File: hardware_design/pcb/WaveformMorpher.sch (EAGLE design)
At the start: 52 parts, among them IC1 MAX11615EEE+, IC2 TL074D, IC3 LM4041B12DBZ, J1 WQP-PJ301M-12_JACK, J2 WQP-PJ301M-12_JACK, J3 WQP-PJ301M-12_JACK, J4 WQP-PJ301M-12_JACK, J5 WQP-PJ301M-12_JACK, T1 MMBT3904

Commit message: Board added
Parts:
- added C10, C11, C12, C7, C8, C9: 100n, rcl:C-USC0603
- added C5: 10u, rcl:CPOL-USB
- added C6: 18p, rcl:C-USC0603
- added IC4: LME49720MAX_NOPB, SamacSys_Parts:LME49720MAX_NOPB
- added J6: OUT_J, MusicThingModular:WQP-PJ301M-12_JACK
- added R24: 6.8k, rcl:R-US_R0603
- added R25, R27: 47k, rcl:R-US_R0603
- added R26: 1.0k, rcl:R-US_R0603
- added VR1: LOOP_CV_POT, MusicThingModular:9MM_SNAP-IN_POT_
- J1: value WQP-PJ301M-12_JACK -> GATE_J
- J2: value WQP-PJ301M-12_JACK -> MORPH_J
- J3: value WQP-PJ301M-12_JACK -> 1V/OCT_J
- J4: value WQP-PJ301M-12_JACK -> LOOP_J
- J5: value WQP-PJ301M-12_JACK -> RASP_IN_J
- VR5: value (none) -> LOOP_POT
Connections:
- removed net 12V: D1.K
- new net +12V: C11.1, D1.K, IC4.V+
- new net N$17: IC4.INPUT_B-, IC4.OUTPUT_B
- new net N$18: C6.2, IC4.OUTPUT_A, R26.1, R27.2
- new net N$19: J5.2, R26.2
- new net N$2: C10.1, C7.1, C8.1, C9.1
- new net N$20: C5.+, J6.2
- new net N$21: C5.-, R24.1, R25.2
- new net N$22: R20.1, VR5.S
- new net N$23: C6.1, IC4.INPUT_A-, R24.2, R27.1
- new net N$24: R23.1, VR1.S
- new net N$3: IC1.REF, IC2A.+IN
- net -12V: now also C12.2, IC4.V-
- net 5V: now also J4.3
- net GND: now also C10.2, C11.2, C12.1, C7.2, C8.2, C9.2, IC2D.+IN, IC4.INPUT_A+, IC4.INPUT_B+, J6.1, R25.1, VR1.A, VR5.A
- net N$12: now also J2.1
- net N$16: now also VR1.E; no longer R23.1
- net VREF2.0: now also IC2A.-IN, IC2A.OUT, VR5.E; no longer IC1.REF, R20.1
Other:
- moved on the sheet: ATTACK_POT, C1, C2, C3, C4, D1, D2, DECAY_POT, IC1, IC2B, IC2C, IC2D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

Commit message: Board first placements
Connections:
- removed net 1V/OCT_ADC1: C3.2, R18.2
- net MORPH_ADC: now also C3.2, R18.2
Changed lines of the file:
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@@
-</segment>
-</net>
-<net name="1V/OCT_ADC1" class="0">
-<segment>
-<pinref part="C3" gate="G$1" pin="2"/>
-<wire x1="76.2" y1="121.92" x2="83.82" y2="121.92" width="0.1524" layer="91"/>
-<wire x1="83.82" y1="121.92" x2="83.82" y2="111.76" width="0.1524" layer="91"/>
-<pinref part="R18" gate="G$1" pin="2"/>
-<wire x1="83.82" y1="111.76" x2="76.2" y2="111.76" width="0.1524" layer="91"/>
-<wire x1="83.82" y1="111.76" x2="83.82" y2="99.06" width="0.1524" layer="91"/>
-<junction x="83.82" y="111.76"/>
 </segment>
 </net>
@@
 <junction x="58.42" y="101.6"/>
 <pinref part="IC2" gate="C" pin="-IN"/>
-</segment>
-</net>
-<net name="MORPH_ADC" class="0">
-<segment>
-<pinref part="IC2" gate="C" pin="OUT"/>
-<wire x1="78.74" y1="99.06" x2="88.9" y2="99.06" width="0.1524" layer="91"/>
-<label x="88.9" y="99.06" size="1.778" layer="95" xref="yes"/>
 </segment>
 </net>
@@
 </segment>
 </net>
+<net name="MORPH_ADC" class="0">
+<segment>
+<pinref part="C3" gate="G$1" pin="2"/>
+<wire x1="76.2" y1="121.92" x2="83.82" y2="121.92" width="0.1524" layer="91"/>
+<wire x1="83.82" y1="121.92" x2="83.82" y2="111.76" width="0.1524" layer="91"/>
+<pinref part="R18" gate="G$1" pin="2"/>
+<wire x1="83.82" y1="111.76" x2="76.2" y2="111.76" width="0.1524" layer="91"/>
+<pinref part="IC2" gate="C" pin="OUT"/>
+<wire x1="78.74" y1="99.06" x2="83.82" y2="99.06" width="0.1524" layer="91"/>
+<label x="88.9" y="99.06" size="1.778" layer="95" xref="yes"/>
+<wire x1="83.82" y1="99.06" x2="88.9" y2="99.06" width="0.1524" layer="91"/>
+<wire x1="83.82" y1="111.76" x2="83.82" y2="99.06" width="0.1524" layer="91"/>
+<junction x="83.82" y="111.76"/>
+<junction x="83.82" y="99.06"/>
+</segment>
+</net>

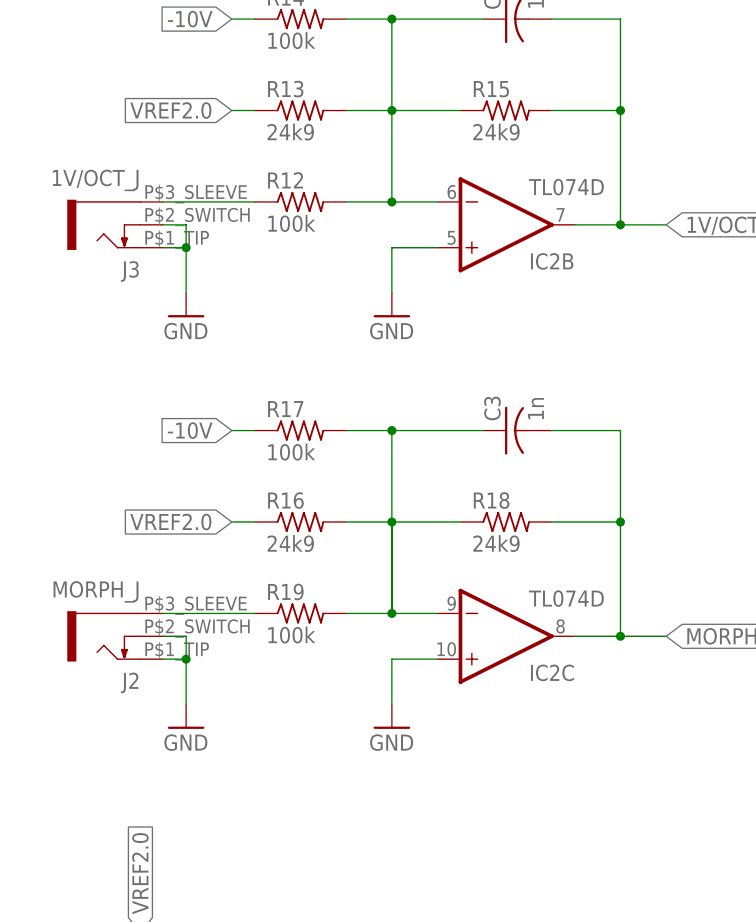
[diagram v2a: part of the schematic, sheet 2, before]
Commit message: adding vias
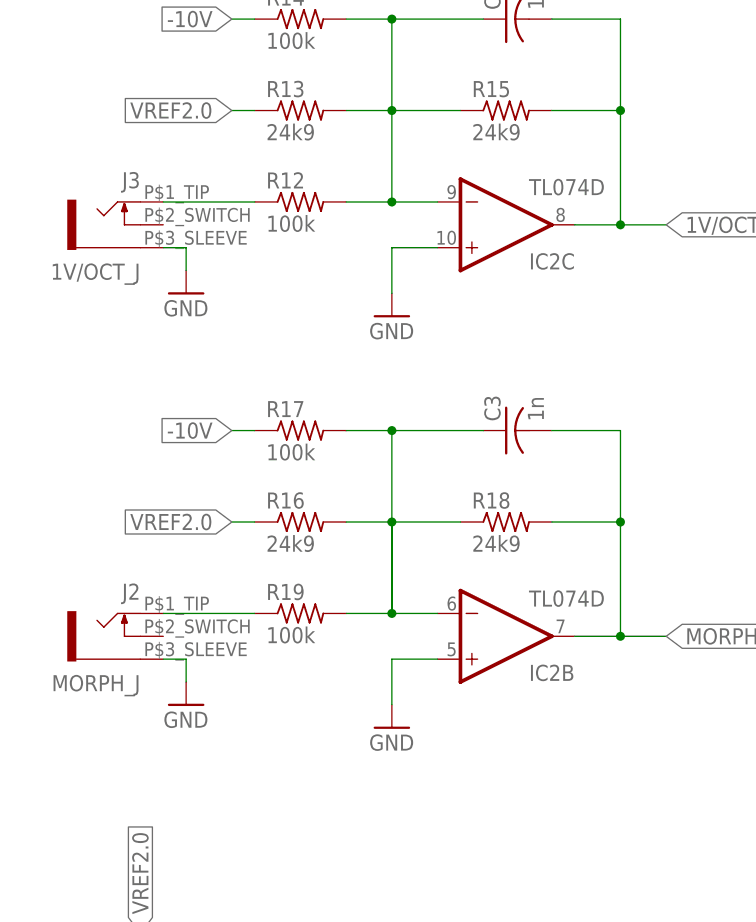
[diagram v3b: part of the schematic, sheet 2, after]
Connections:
- removed net N$13: IC2C.-IN, R19.2
- net 1V/OCT_ADC: now also IC2C.OUT; no longer IC2B.OUT
- net GND: now also J2.1, J3.1; no longer J2.2, J2.3, J3.2, J3.3
- net MORPH_ADC: now also IC2B.OUT; no longer IC2C.OUT
- net N$10: now also IC2B.-IN, R19.2
- net N$12: now also J3.2, R12.1; no longer J2.1, R19.1
- net N$8: now also J2.2, R19.1; no longer J3.1, R12.1
- net N$9: now also IC2C.-IN; no longer IC2B.-IN
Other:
- moved on the sheet: IC2B, IC2C, J2, J3
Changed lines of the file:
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@@
 <part name="GND5" library="supply1" deviceset="GND" device=""/>
 <part name="GND6" library="supply1" deviceset="GND" device=""/>
-<part name="GND7" library="supply1" deviceset="GND" device=""/>
-<part name="GND8" library="supply1" deviceset="GND" device=""/>
 <part name="GND9" library="supply1" deviceset="GND" device=""/>
 <part name="GND10" library="supply1" deviceset="GND" device=""/>
@@
 <part name="VR1" library="MusicThingModular" deviceset="9MM_SNAP-IN_POT" device="_" value="LOOP_CV_POT"/>
 <part name="GND36" library="supply1" deviceset="GND" device=""/>
+<part name="GND7" library="supply1" deviceset="GND" device=""/>
+<part name="GND8" library="supply1" deviceset="GND" device=""/>
 </parts>
 <sheets>
@@
 <instances>
 <instance part="J5" gate="G$1" x="124.46" y="78.74" rot="MR0"/>
-<instance part="J3" gate="G$1" x="27.94" y="144.78" rot="R180"/>
-<instance part="J2" gate="G$1" x="27.94" y="99.06" rot="R180"/>
+<instance part="J3" gate="G$1" x="27.94" y="144.78" rot="MR0"/>
+<instance part="J2" gate="G$1" x="27.94" y="99.06" rot="MR0"/>
 <instance part="J1" gate="G$1" x="200.66" y="116.84" rot="MR0"/>
 <instance part="J4" gate="G$1" x="25.4" y="33.02" rot="MR0"/>
@@
 <instance part="GND5" gate="1" x="134.62" y="68.58" rot="MR0"/>
 <instance part="GND6" gate="1" x="33.02" y="22.86"/>
-<instance part="GND7" gate="1" x="35.56" y="134.62"/>
-<instance part="GND8" gate="1" x="35.56" y="88.9"/>
 <instance part="GND9" gate="1" x="208.28" y="106.68"/>
-<instance part="IC2" gate="B" x="71.12" y="144.78" rot="MR180"/>
-<instance part="IC2" gate="C" x="71.12" y="99.06" rot="MR180"/>
+<instance part="IC2" gate="B" x="71.12" y="99.06" rot="MR180"/>
+<instance part="IC2" gate="C" x="71.12" y="144.78" rot="MR180"/>
 <instance part="IC2" gate="D" x="86.36" y="33.02" rot="MR180"/>
 <instance part="I/O" gate="G$1" x="-5.08" y="0">
@@
 <instance part="VR1" gate="G$1" x="48.26" y="30.48"/>
 <instance part="GND36" gate="1" x="48.26" y="17.78"/>
+<instance part="GND7" gate="1" x="35.56" y="137.16"/>
+<instance part="GND8" gate="1" x="35.56" y="91.44"/>
 </instances>
 <busses>
@@
 <pinref part="GND6" gate="1" pin="GND"/>
 <pinref part="J4" gate="G$1" pin="1"/>
-</segment>
-<segment>
-<wire x1="33.02" y1="142.24" x2="35.56" y2="142.24" width="0.1524" layer="91"/>
-<wire x1="35.56" y1="142.24" x2="35.56" y2="137.16" width="0.1524" layer="91"/>
-<pinref part="GND7" gate="1" pin="GND"/>
-<pinref part="J3" gate="G$1" pin="2"/>
-<pinref part="J3" gate="G$1" pin="3"/>
-<wire x1="33.02" y1="144.78" x2="35.56" y2="144.78" width="0.1524" layer="91"/>
-<wire x1="35.56" y1="144.78" x2="35.56" y2="142.24" width="0.1524" layer="91"/>
-<junction x="35.56" y="142.24"/>
-</segment>
-<segment>
-<wire x1="33.02" y1="96.52" x2="35.56" y2="96.52" width="0.1524" layer="91"/>
-<wire x1="35.56" y1="96.52" x2="35.56" y2="91.44" width="0.1524" layer="91"/>
-<pinref part="GND8" gate="1" pin="GND"/>
-<pinref part="J2" gate="G$1" pin="2"/>
-<pinref part="J2" gate="G$1" pin="3"/>
-<wire x1="33.02" y1="99.06" x2="35.56" y2="99.06" width="0.1524" layer="91"/>
-<wire x1="35.56" y1="99.06" x2="35.56" y2="96.52" width="0.1524" layer="91"/>
-<junction x="35.56" y="96.52"/>
 </segment>
 <segment>
@@
 </segment>
 <segment>
-<pinref part="IC2" gate="B" pin="+IN"/>
-<wire x1="63.5" y1="142.24" x2="58.42" y2="142.24" width="0.1524" layer="91"/>
 <wire x1="58.42" y1="142.24" x2="58.42" y2="137.16" width="0.1524" layer="91"/>
 <pinref part="GND25" gate="1" pin="GND"/>
-</segment>
-<segment>
-<wire x1="63.5" y1="96.52" x2="58.42" y2="96.52" width="0.1524" layer="91"/>
+<pinref part="IC2" gate="C" pin="+IN"/>
+<wire x1="63.5" y1="142.24" x2="58.42" y2="142.24" width="0.1524" layer="91"/>
+</segment>
+<segment>
 <wire x1="58.42" y1="96.52" x2="58.42" y2="91.44" width="0.1524" layer="91"/>
 <pinref part="GND26" gate="1" pin="GND"/>
-<pinref part="IC2" gate="C" pin="+IN"/>
+<pinref part="IC2" gate="B" pin="+IN"/>
+<wire x1="63.5" y1="96.52" x2="58.42" y2="96.52" width="0.1524" layer="91"/>
 </segment>
 <segment>
@@
 <wire x1="48.26" y1="22.86" x2="48.26" y2="20.32" width="0.1524" layer="91"/>
 <pinref part="GND36" gate="1" pin="GND"/>
+</segment>
+<segment>
+<pinref part="J3" gate="G$1" pin="1"/>
+<wire x1="33.02" y1="142.24" x2="35.56" y2="142.24" width="0.1524" layer="91"/>
+<wire x1="35.56" y1="142.24" x2="35.56" y2="139.7" width="0.1524" layer="91"/>
+<pinref part="GND7" gate="1" pin="GND"/>
+</segment>
+<segment>
+<pinref part="J2" gate="G$1" pin="1"/>
+<wire x1="33.02" y1="96.52" x2="35.56" y2="96.52" width="0.1524" layer="91"/>
+<wire x1="35.56" y1="96.52" x2="35.56" y2="93.98" width="0.1524" layer="91"/>
+<pinref part="GND8" gate="1" pin="GND"/>
 </segment>
 </net>
@@
 </segment>
 </net>
-<net name="N$8" class="0">
-<segment>
-<pinref part="J3" gate="G$1" pin="1"/>
-<pinref part="R12" gate="G$1" pin="1"/>
-<wire x1="33.02" y1="147.32" x2="43.18" y2="147.32" width="0.1524" layer="91"/>
-</segment>
-</net>
 <net name="N$9" class="0">
 <segment>
 <pinref part="R12" gate="G$1" pin="2"/>
 <wire x1="53.34" y1="147.32" x2="58.42" y2="147.32" width="0.1524" layer="91"/>
-<wire x1="58.42" y1="147.32" x2="63.5" y2="147.32" width="0.1524" layer="91"/>
 <wire x1="58.42" y1="147.32" x2="58.42" y2="157.48" width="0.1524" layer="91"/>
-<junction x="58.42" y="147.32"/>
 <pinref part="R13" gate="G$1" pin="2"/>
 <wire x1="58.42" y1="157.48" x2="53.34" y2="157.48" width="0.1524" layer="91"/>
@@
 <pinref part="R14" gate="G$1" pin="2"/>
 <wire x1="58.42" y1="167.64" x2="53.34" y2="167.64" width="0.1524" layer="91"/>
-<pinref part="IC2" gate="B" pin="-IN"/>
 <pinref part="R15" gate="G$1" pin="1"/>
 <wire x1="58.42" y1="157.48" x2="66.04" y2="157.48" width="0.1524" layer="91"/>
@@
 <wire x1="58.42" y1="167.64" x2="68.58" y2="167.64" width="0.1524" layer="91"/>
 <junction x="58.42" y="167.64"/>
+<pinref part="IC2" gate="C" pin="-IN"/>
+<wire x1="58.42" y1="147.32" x2="63.5" y2="147.32" width="0.1524" layer="91"/>
+<junction x="58.42" y="147.32"/>
 </segment>
 </net>
@@
 <wire x1="83.82" y1="157.48" x2="83.82" y2="144.78" width="0.1524" layer="91"/>
 <junction x="83.82" y="157.48"/>
-<pinref part="IC2" gate="B" pin="OUT"/>
+<wire x1="83.82" y1="144.78" x2="88.9" y2="144.78" width="0.1524" layer="91"/>
+<label x="88.9" y="144.78" size="1.778" layer="95" xref="yes"/>
+<pinref part="IC2" gate="C" pin="OUT"/>
 <wire x1="78.74" y1="144.78" x2="83.82" y2="144.78" width="0.1524" layer="91"/>
-<wire x1="83.82" y1="144.78" x2="88.9" y2="144.78" width="0.1524" layer="91"/>
 <junction x="83.82" y="144.78"/>
-<label x="88.9" y="144.78" size="1.778" layer="95" xref="yes"/>
 </segment>
 </net>
@@
 <wire x1="58.42" y1="121.92" x2="68.58" y2="121.92" width="0.1524" layer="91"/>
 <junction x="58.42" y="121.92"/>
-</segment>
-</net>
-<net name="N$12" class="0">
-<segment>
-<pinref part="R19" gate="G$1" pin="1"/>
-<wire x1="33.02" y1="101.6" x2="43.18" y2="101.6" width="0.1524" layer="91"/>
-<pinref part="J2" gate="G$1" pin="1"/>
-</segment>
-</net>
-<net name="N$13" class="0">
-<segment>
+<pinref part="IC2" gate="B" pin="-IN"/>
+<wire x1="63.5" y1="101.6" x2="58.42" y2="101.6" width="0.1524" layer="91"/>
 <pinref part="R19" gate="G$1" pin="2"/>
 <wire x1="53.34" y1="101.6" x2="58.42" y2="101.6" width="0.1524" layer="91"/>
-<wire x1="58.42" y1="101.6" x2="63.5" y2="101.6" width="0.1524" layer="91"/>
+<junction x="58.42" y="101.6"/>
+</segment>
+</net>
+<net name="N$13" class="0">
+<segment>
 <wire x1="58.42" y1="101.6" x2="58.42" y2="111.76" width="0.1524" layer="91"/>
-<junction x="58.42" y="101.6"/>
-<pinref part="IC2" gate="C" pin="-IN"/>
 </segment>
 </net>
@@
 <pinref part="R18" gate="G$1" pin="2"/>
 <wire x1="83.82" y1="111.76" x2="76.2" y2="111.76" width="0.1524" layer="91"/>
-<pinref part="IC2" gate="C" pin="OUT"/>
-<wire x1="78.74" y1="99.06" x2="83.82" y2="99.06" width="0.1524" layer="91"/>
 <label x="88.9" y="99.06" size="1.778" layer="95" xref="yes"/>
 <wire x1="83.82" y1="99.06" x2="88.9" y2="99.06" width="0.1524" layer="91"/>
 <wire x1="83.82" y1="111.76" x2="83.82" y2="99.06" width="0.1524" layer="91"/>
 <junction x="83.82" y="111.76"/>
+<pinref part="IC2" gate="B" pin="OUT"/>
+<wire x1="78.74" y1="99.06" x2="83.82" y2="99.06" width="0.1524" layer="91"/>
 <junction x="83.82" y="99.06"/>
 </segment>
 </net>
+<net name="N$8" class="0">
+<segment>
+<pinref part="J2" gate="G$1" pin="2"/>
+<pinref part="R19" gate="G$1" pin="1"/>
+<wire x1="33.02" y1="101.6" x2="43.18" y2="101.6" width="0.1524" layer="91"/>
+</segment>
+</net>
+<net name="N$12" class="0">
+<segment>
+<pinref part="J3" gate="G$1" pin="2"/>
+<pinref part="R12" gate="G$1" pin="1"/>
+<wire x1="33.02" y1="147.32" x2="43.18" y2="147.32" width="0.1524" layer="91"/>
+</segment>
+</net>

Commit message: finishing up the board
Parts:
- removed C7, C9: 100n, rcl:C-USC0603
- P1, P2, P3, P4: value (none) -> 10kB
- P5: value LOOP_POT -> 10kB
- P6: value LOOP_CV_POT -> 10kB
- renumbered ATTACK_POT to P1, DECAY_POT to P2, RELEASE_POT to P4, SUSTAIN_POT to P3, VR1 to P6, VR5 to P5
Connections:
- removed net N$2: C10.1, C7.1, C8.1, C9.1
- net 3.3V: now also C10.1, C8.1, IC2P.V+
- net GND: now also IC2P.V-; no longer C7.2, C9.2
- net N$11: now also D1.A, JP1.10; no longer D2.K
- net N$7: now also D2.K, JP1.2; no longer D1.A
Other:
- moved on the sheet: C8, D1, D2, IC3

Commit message: hardware v0.7
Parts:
- IC2: value TL074D -> MCP6004
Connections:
- net GATE_ADC renamed GATE_GPIO
- net SW7_GPIO renamed SW7_ADC
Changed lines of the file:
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@@
 <part name="R7" library="rcl" deviceset="R-US_" device="R0603" value="10k"/>
 <part name="GND22" library="supply1" deviceset="GND" device=""/>
-<part name="IC2" library="gm-ics" deviceset="TL074" device="D"/>
+<part name="IC2" library="gm-ics" deviceset="TL074" device="D" value="MCP6004"/>
 <part name="IC3" library="texas" deviceset="LM4041" device="DBZ" technology="B12"/>
 <part name="R8" library="rcl" deviceset="R-US_" device="R0603" value="1.0k"/>
@@
 <part name="I/O" library="SparkFun-Aesthetics" deviceset="FRAME-A4L" device="">
 <attribute name="CNAME" value="I/O"/>
+<attribute name="CREVISION" value="0.7"/>
 <attribute name="DESIGNER" value="Kristóf Kónya"/>
-<attribute name="REV" value="1.0"/>
+<attribute name="REV" value="0.7"/>
 </part>
 <part name="FRAME2" library="SparkFun-Aesthetics" deviceset="FRAME-A4L" device="">
 <attribute name="CNAME" value="POWER/DAC/CON"/>
+<attribute name="CREVISION" value="0.7"/>
 <attribute name="DESIGNER" value="Kristóf Kónya"/>
-<attribute name="REV" value="1.0"/>
+<attribute name="REV" value="0.7"/>
 </part>
 <part name="FRAME3" library="SparkFun-Aesthetics" deviceset="FRAME-A4L" device="">
 <attribute name="CNAME" value="SWITCHES/POTS"/>
+<attribute name="CREVISION" value="0.7"/>
 <attribute name="DESIGNER" value="Kristóf Kónya"/>
-<attribute name="REV" value="1.0"/>
+<attribute name="REV" value="0.7"/>
 </part>
 <part name="R1" library="rcl" deviceset="R-US_" device="R0603" value="10k"/>
@@
 <instance part="FRAME2" gate="G$1" x="-2.54" y="71.12">
 <attribute name="CNAME" x="-2.54" y="71.12" size="1.778" layer="96" display="off"/>
+<attribute name="CREVISION" x="-2.54" y="71.12" size="1.778" layer="96" display="off"/>
 </instance>
 <instance part="IC2" gate="A" x="58.42" y="182.88"/>
@@
 </segment>
 </net>
-<net name="GATE_ADC" class="0">
+<net name="GATE_GPIO" class="0">
 <segment>
 <pinref part="RASPI" gate="G$1" pin="16"/>
@@
 </segment>
 </net>
-<net name="SW7_GPIO" class="0">
+<net name="SW7_ADC" class="0">
 <segment>
 <pinref part="IC1" gate="G$1" pin="AIN5"/>
@@
 <instance part="I/O" gate="G$1" x="-5.08" y="0">
 <attribute name="CNAME" x="-5.08" y="0" size="1.778" layer="96" display="off"/>
+<attribute name="CREVISION" x="-5.08" y="0" size="1.778" layer="96" display="off"/>
 </instance>
 <instance part="R10" gate="G$1" x="220.98" y="119.38" rot="R180"/>
@@
 </segment>
 </net>
-<net name="GATE_ADC" class="0">
+<net name="GATE_GPIO" class="0">
 <segment>
 <pinref part="T1" gate="G$1" pin="C"/>
@@
 <instance part="FRAME3" gate="G$1" x="-17.78" y="-10.16">
 <attribute name="CNAME" x="-17.78" y="-10.16" size="1.778" layer="96" display="off"/>
+<attribute name="CREVISION" x="-17.78" y="-10.16" size="1.778" layer="96" display="off"/>
 </instance>
 <instance part="S1" gate="G$1" x="30.48" y="152.4" rot="MR180"/>
@@
 </segment>
 </net>
-<net name="SW7_GPIO" class="0">
+<net name="SW7_ADC" class="0">
 <segment>
 <pinref part="S7" gate="G$1" pin="2"/>

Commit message: partlist and bugfixes
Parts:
- IC3: value LM4041B12DBZ -> LM4040B10
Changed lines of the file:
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@@
 <part name="GND22" library="supply1" deviceset="GND" device=""/>
 <part name="IC2" library="gm-ics" deviceset="TL074" device="D" value="MCP6004"/>
-<part name="IC3" library="texas" deviceset="LM4041" device="DBZ" technology="B12"/>
+<part name="IC3" library="texas" deviceset="LM4041" device="DBZ" technology="B12" value="LM4040B10"/>
 <part name="R8" library="rcl" deviceset="R-US_" device="R0603" value="1.0k"/>
 <part name="R9" library="rcl" deviceset="R-US_" device="R0603" value="1.0k"/>
